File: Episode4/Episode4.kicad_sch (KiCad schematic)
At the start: 41 parts, among them J1 CARD, J10 CARD, J11 CARD, J12 CARD, J13 CARD, J14 CARD, J2 CARD, J3 CARD, J4 CARD, J5 CARD, J6 CARD, J7 BB Con, J8 ATX POWER, J9 CARD, SW1 POWER, U1 74HCT14, U2 74HCT74

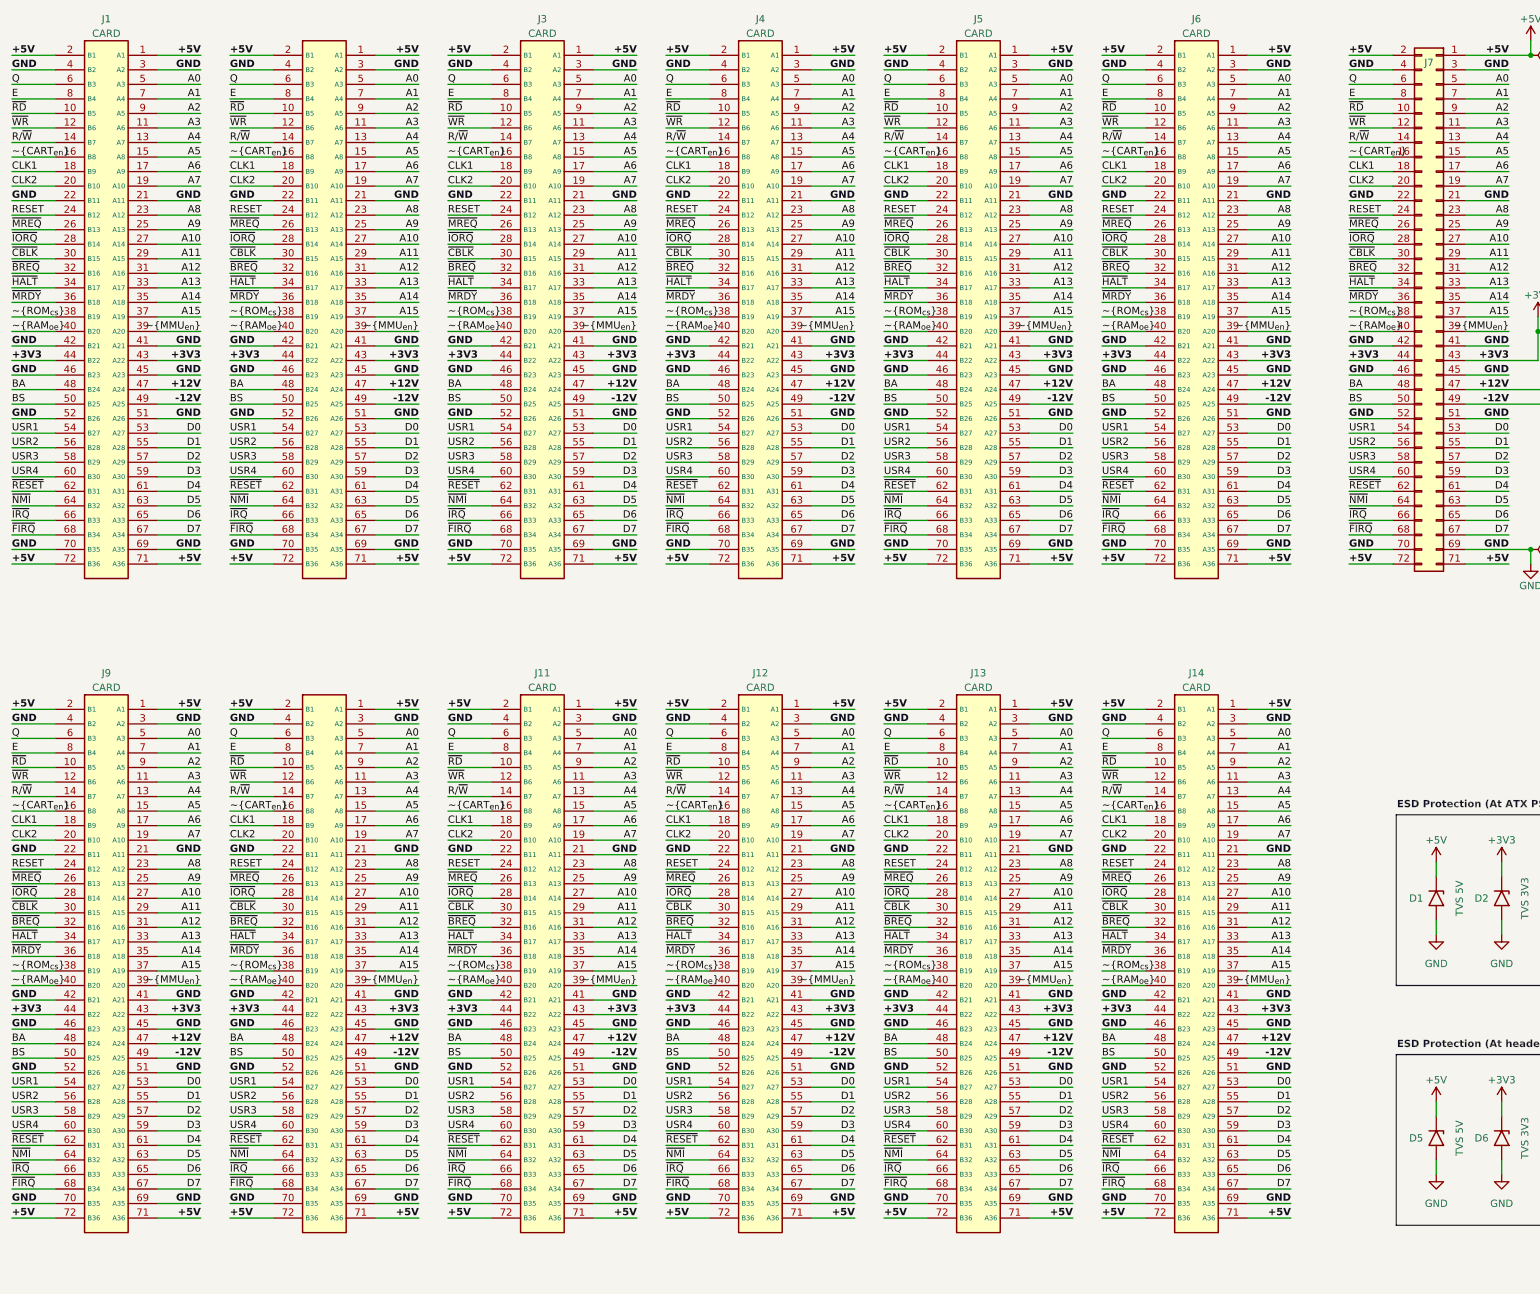
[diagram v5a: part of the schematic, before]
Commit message: Added various IRQ and FIRQ lines
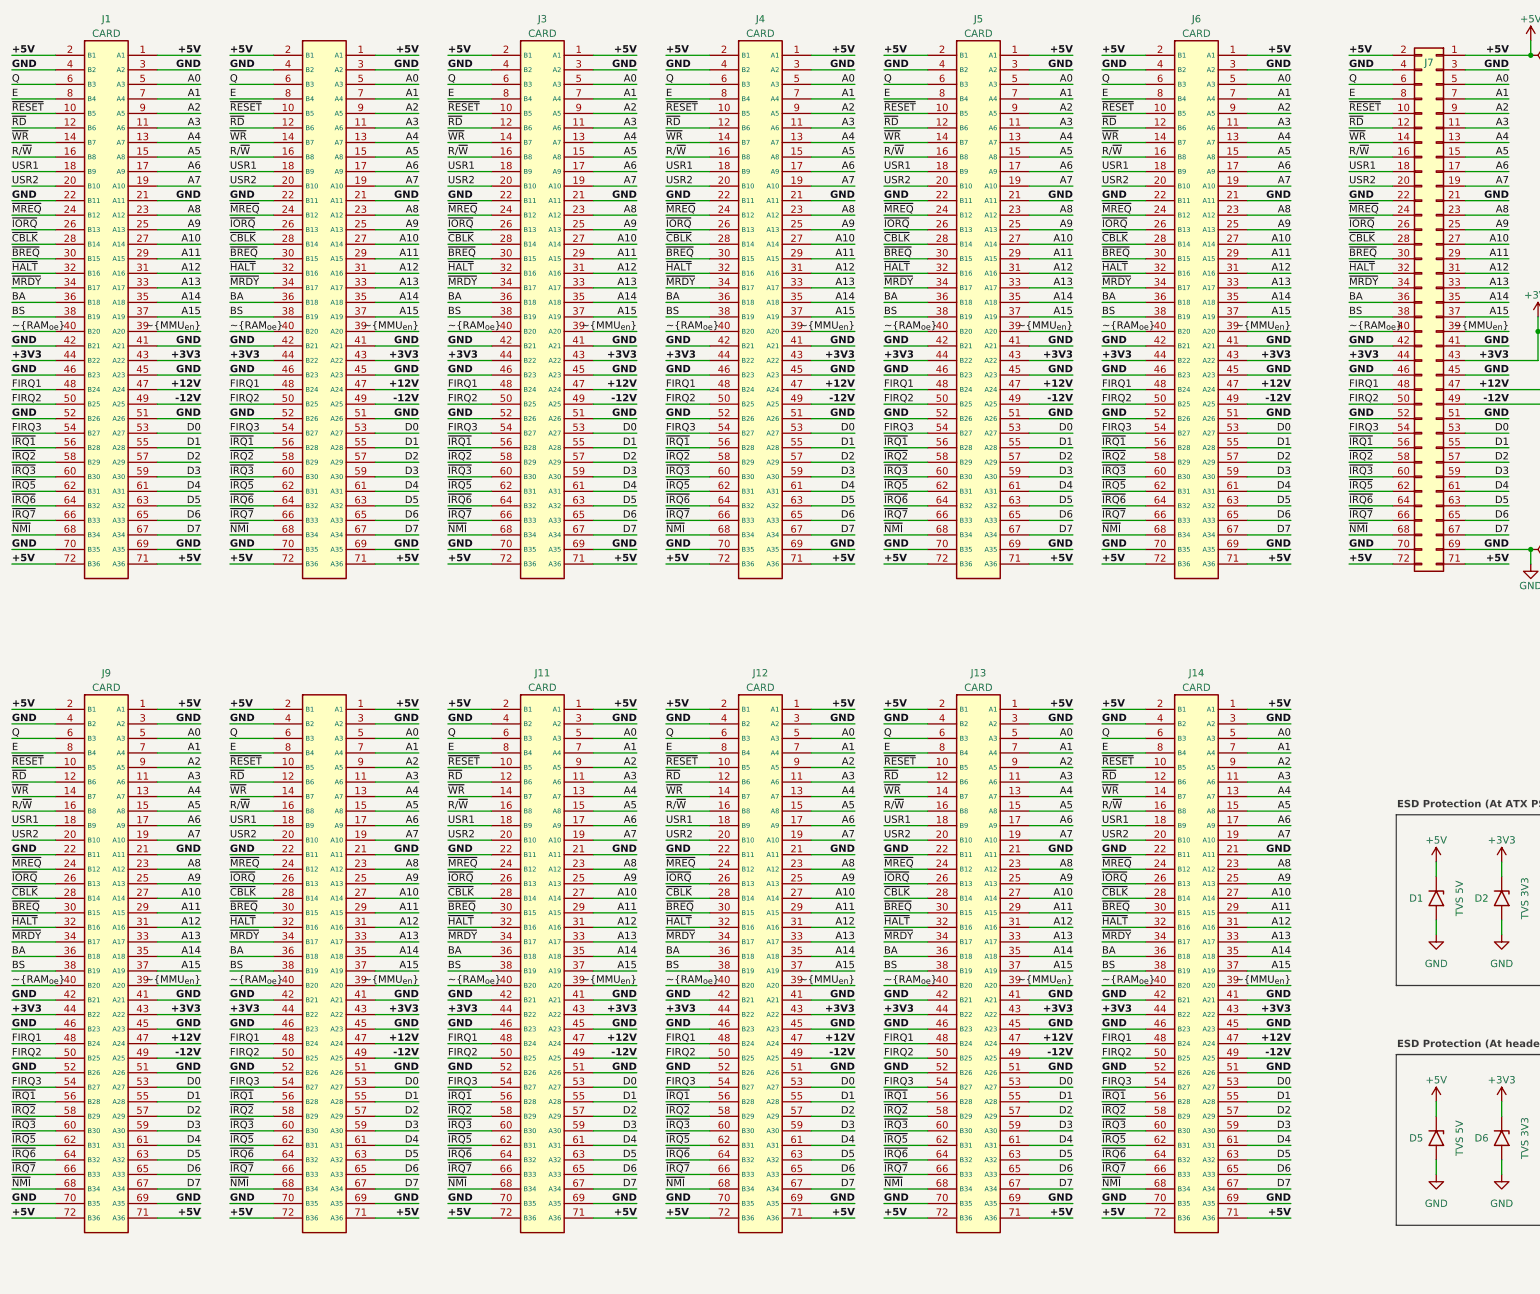
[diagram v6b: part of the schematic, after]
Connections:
- net CLK1 is gone; now on net USR1: J1.18 (B9), J10.18 (B9), J11.18 (B9), J12.18 (B9), J13.18 (B9), J14.18 (B9), J2.18 (B9), J3.18 (B9), J4.18 (B9), J5.18 (B9), J6.18 (B9), J7.18 (Pin_18), J9.18 (B9)
- net CLK2 is gone; now on net USR2: J1.20 (B10), J10.20 (B10), J11.20 (B10), J12.20 (B10), J13.20 (B10), J14.20 (B10), J2.20 (B10), J3.20 (B10), J4.20 (B10), J5.20 (B10), J6.20 (B10), J7.20 (Pin_20), J9.20 (B10)
- net RESET is gone; now on net ~{MREQ}: J1.24 (B12), J10.24 (B12), J11.24 (B12), J12.24 (B12), J13.24 (B12), J14.24 (B12), J2.24 (B12), J3.24 (B12), J4.24 (B12), J5.24 (B12), J6.24 (B12), J7.24 (Pin_24), J9.24 (B12)
- net ~{CART_{en}} is gone; now on net R/~{W}: J1.16 (B8), J10.16 (B8), J11.16 (B8), J12.16 (B8), J13.16 (B8), J14.16 (B8), J2.16 (B8), J3.16 (B8), J4.16 (B8), J5.16 (B8), J6.16 (B8), J7.16 (Pin_16), J9.16 (B8)
- net ~{FIRQ} is gone; now on net ~{NMI}: J1.68 (B34), J10.68 (B34), J11.68 (B34), J12.68 (B34), J13.68 (B34), J14.68 (B34), J2.68 (B34), J3.68 (B34), J4.68 (B34), J5.68 (B34), J6.68 (B34), J7.68 (Pin_68), J9.68 (B34)
- net ~{ROM_{cs}} is gone; now on net BS: J1.38 (B19), J10.38 (B19), J11.38 (B19), J12.38 (B19), J13.38 (B19), J14.38 (B19), J2.38 (B19), J3.38 (B19), J4.38 (B19), J5.38 (B19), J6.38 (B19), J7.38 (Pin_38), J9.38 (B19)
- net BA: now also J1.36 (B18), J10.36 (B18), J11.36 (B18), J12.36 (B18), J13.36 (B18), J14.36 (B18), J2.36 (B18), J3.36 (B18), J4.36 (B18), J5.36 (B18), J6.36 (B18), J7.36 (Pin_36), J9.36 (B18); no longer J1.48 (B24), J10.48 (B24), J11.48 (B24), J12.48 (B24), J13.48 (B24), J14.48 (B24), J2.48 (B24), J3.48 (B24), J4.48 (B24), J5.48 (B24), J6.48 (B24), J7.48 (Pin_48), J9.48 (B24)
- net BS: no longer J1.50 (B25), J10.50 (B25), J11.50 (B25), J12.50 (B25), J13.50 (B25), J14.50 (B25), J2.50 (B25), J3.50 (B25), J4.50 (B25), J5.50 (B25), J6.50 (B25), J7.50 (Pin_50), J9.50 (B25)
- net R/~{W}: no longer J1.14 (B7), J10.14 (B7), J11.14 (B7), J12.14 (B7), J13.14 (B7), J14.14 (B7), J2.14 (B7), J3.14 (B7), J4.14 (B7), J5.14 (B7), J6.14 (B7), J7.14 (Pin_14), J9.14 (B7)
- net USR1: no longer J1.54 (B27), J10.54 (B27), J11.54 (B27), J12.54 (B27), J13.54 (B27), J14.54 (B27), J2.54 (B27), J3.54 (B27), J4.54 (B27), J5.54 (B27), J6.54 (B27), J7.54 (Pin_54), J9.54 (B27)
- net USR2: no longer J1.56 (B28), J10.56 (B28), J11.56 (B28), J12.56 (B28), J13.56 (B28), J14.56 (B28), J2.56 (B28), J3.56 (B28), J4.56 (B28), J5.56 (B28), J6.56 (B28), J7.56 (Pin_56), J9.56 (B28)
- net ~{BREQ}: now also J1.30 (B15), J10.30 (B15), J11.30 (B15), J12.30 (B15), J13.30 (B15), J14.30 (B15), J2.30 (B15), J3.30 (B15), J4.30 (B15), J5.30 (B15), J6.30 (B15), J7.30 (Pin_30), J9.30 (B15); no longer J1.32 (B16), J10.32 (B16), J11.32 (B16), J12.32 (B16), J13.32 (B16), J14.32 (B16), J2.32 (B16), J3.32 (B16), J4.32 (B16), J5.32 (B16), J6.32 (B16), J7.32 (Pin_32), J9.32 (B16)
- net ~{CBLK}: now also J1.28 (B14), J10.28 (B14), J11.28 (B14), J12.28 (B14), J13.28 (B14), J14.28 (B14), J2.28 (B14), J3.28 (B14), J4.28 (B14), J5.28 (B14), J6.28 (B14), J7.28 (Pin_28), J9.28 (B14); no longer J1.30 (B15), J10.30 (B15), J11.30 (B15), J12.30 (B15), J13.30 (B15), J14.30 (B15), J2.30 (B15), J3.30 (B15), J4.30 (B15), J5.30 (B15), J6.30 (B15), J7.30 (Pin_30), J9.30 (B15)
- net ~{HALT}: now also J1.32 (B16), J10.32 (B16), J11.32 (B16), J12.32 (B16), J13.32 (B16), J14.32 (B16), J2.32 (B16), J3.32 (B16), J4.32 (B16), J5.32 (B16), J6.32 (B16), J7.32 (Pin_32), J9.32 (B16); no longer J1.34 (B17), J10.34 (B17), J11.34 (B17), J12.34 (B17), J13.34 (B17), J14.34 (B17), J2.34 (B17), J3.34 (B17), J4.34 (B17), J5.34 (B17), J6.34 (B17), J7.34 (Pin_34), J9.34 (B17)
- net ~{IORQ}: now also J1.26 (B13), J10.26 (B13), J11.26 (B13), J12.26 (B13), J13.26 (B13), J14.26 (B13), J2.26 (B13), J3.26 (B13), J4.26 (B13), J5.26 (B13), J6.26 (B13), J7.26 (Pin_26), J9.26 (B13); no longer J1.28 (B14), J10.28 (B14), J11.28 (B14), J12.28 (B14), J13.28 (B14), J14.28 (B14), J2.28 (B14), J3.28 (B14), J4.28 (B14), J5.28 (B14), J6.28 (B14), J7.28 (Pin_28), J9.28 (B14)
- net ~{MRDY}: now also J1.34 (B17), J10.34 (B17), J11.34 (B17), J12.34 (B17), J13.34 (B17), J14.34 (B17), J2.34 (B17), J3.34 (B17), J4.34 (B17), J5.34 (B17), J6.34 (B17), J7.34 (Pin_34), J9.34 (B17); no longer J1.36 (B18), J10.36 (B18), J11.36 (B18), J12.36 (B18), J13.36 (B18), J14.36 (B18), J2.36 (B18), J3.36 (B18), J4.36 (B18), J5.36 (B18), J6.36 (B18), J7.36 (Pin_36), J9.36 (B18)
- net ~{MREQ}: no longer J1.26 (B13), J10.26 (B13), J11.26 (B13), J12.26 (B13), J13.26 (B13), J14.26 (B13), J2.26 (B13), J3.26 (B13), J4.26 (B13), J5.26 (B13), J6.26 (B13), J7.26 (Pin_26), J9.26 (B13)
- net ~{NMI}: no longer J1.64 (B32), J10.64 (B32), J11.64 (B32), J12.64 (B32), J13.64 (B32), J14.64 (B32), J2.64 (B32), J3.64 (B32), J4.64 (B32), J5.64 (B32), J6.64 (B32), J7.64 (Pin_64), J9.64 (B32)
- net ~{RD}: now also J1.12 (B6), J10.12 (B6), J11.12 (B6), J12.12 (B6), J13.12 (B6), J14.12 (B6), J2.12 (B6), J3.12 (B6), J4.12 (B6), J5.12 (B6), J6.12 (B6), J7.12 (Pin_12), J9.12 (B6); no longer J1.10 (B5), J10.10 (B5), J11.10 (B5), J12.10 (B5), J13.10 (B5), J14.10 (B5), J2.10 (B5), J3.10 (B5), J4.10 (B5), J5.10 (B5), J6.10 (B5), J7.10 (Pin_10), J9.10 (B5)
- net ~{RESET}: now also J1.10 (B5), J10.10 (B5), J11.10 (B5), J12.10 (B5), J13.10 (B5), J14.10 (B5), J2.10 (B5), J3.10 (B5), J4.10 (B5), J5.10 (B5), J6.10 (B5), J7.10 (Pin_10), J9.10 (B5); no longer J1.62 (B31), J10.62 (B31), J11.62 (B31), J12.62 (B31), J13.62 (B31), J14.62 (B31), J2.62 (B31), J3.62 (B31), J4.62 (B31), J5.62 (B31), J6.62 (B31), J7.62 (Pin_62), J9.62 (B31)
- net ~{WR}: now also J1.14 (B7), J10.14 (B7), J11.14 (B7), J12.14 (B7), J13.14 (B7), J14.14 (B7), J2.14 (B7), J3.14 (B7), J4.14 (B7), J5.14 (B7), J6.14 (B7), J7.14 (Pin_14), J9.14 (B7); no longer J1.12 (B6), J10.12 (B6), J11.12 (B6), J12.12 (B6), J13.12 (B6), J14.12 (B6), J2.12 (B6), J3.12 (B6), J4.12 (B6), J5.12 (B6), J6.12 (B6), J7.12 (Pin_12), J9.12 (B6)
- net USR3 renamed ~{IRQ2}
- net USR4 renamed ~{IRQ3}
- net ~{IRQ} renamed ~{IRQ7}
- new net FIRQ1: J1.48 (B24), J10.48 (B24), J11.48 (B24), J12.48 (B24), J13.48 (B24), J14.48 (B24), J2.48 (B24), J3.48 (B24), J4.48 (B24), J5.48 (B24), J6.48 (B24), J7.48 (Pin_48), J9.48 (B24)
- new net FIRQ2: J1.50 (B25), J10.50 (B25), J11.50 (B25), J12.50 (B25), J13.50 (B25), J14.50 (B25), J2.50 (B25), J3.50 (B25), J4.50 (B25), J5.50 (B25), J6.50 (B25), J7.50 (Pin_50), J9.50 (B25)
- new net FIRQ3: J1.54 (B27), J10.54 (B27), J11.54 (B27), J12.54 (B27), J13.54 (B27), J14.54 (B27), J2.54 (B27), J3.54 (B27), J4.54 (B27), J5.54 (B27), J6.54 (B27), J7.54 (Pin_54), J9.54 (B27)
- new net ~{IRQ1}: J1.56 (B28), J10.56 (B28), J11.56 (B28), J12.56 (B28), J13.56 (B28), J14.56 (B28), J2.56 (B28), J3.56 (B28), J4.56 (B28), J5.56 (B28), J6.56 (B28), J7.56 (Pin_56), J9.56 (B28)
- new net ~{IRQ5}: J1.62 (B31), J10.62 (B31), J11.62 (B31), J12.62 (B31), J13.62 (B31), J14.62 (B31), J2.62 (B31), J3.62 (B31), J4.62 (B31), J5.62 (B31), J6.62 (B31), J7.62 (Pin_62), J9.62 (B31)
- new net ~{IRQ6}: J1.64 (B32), J10.64 (B32), J11.64 (B32), J12.64 (B32), J13.64 (B32), J14.64 (B32), J2.64 (B32), J3.64 (B32), J4.64 (B32), J5.64 (B32), J6.64 (B32), J7.64 (Pin_64), J9.64 (B32)

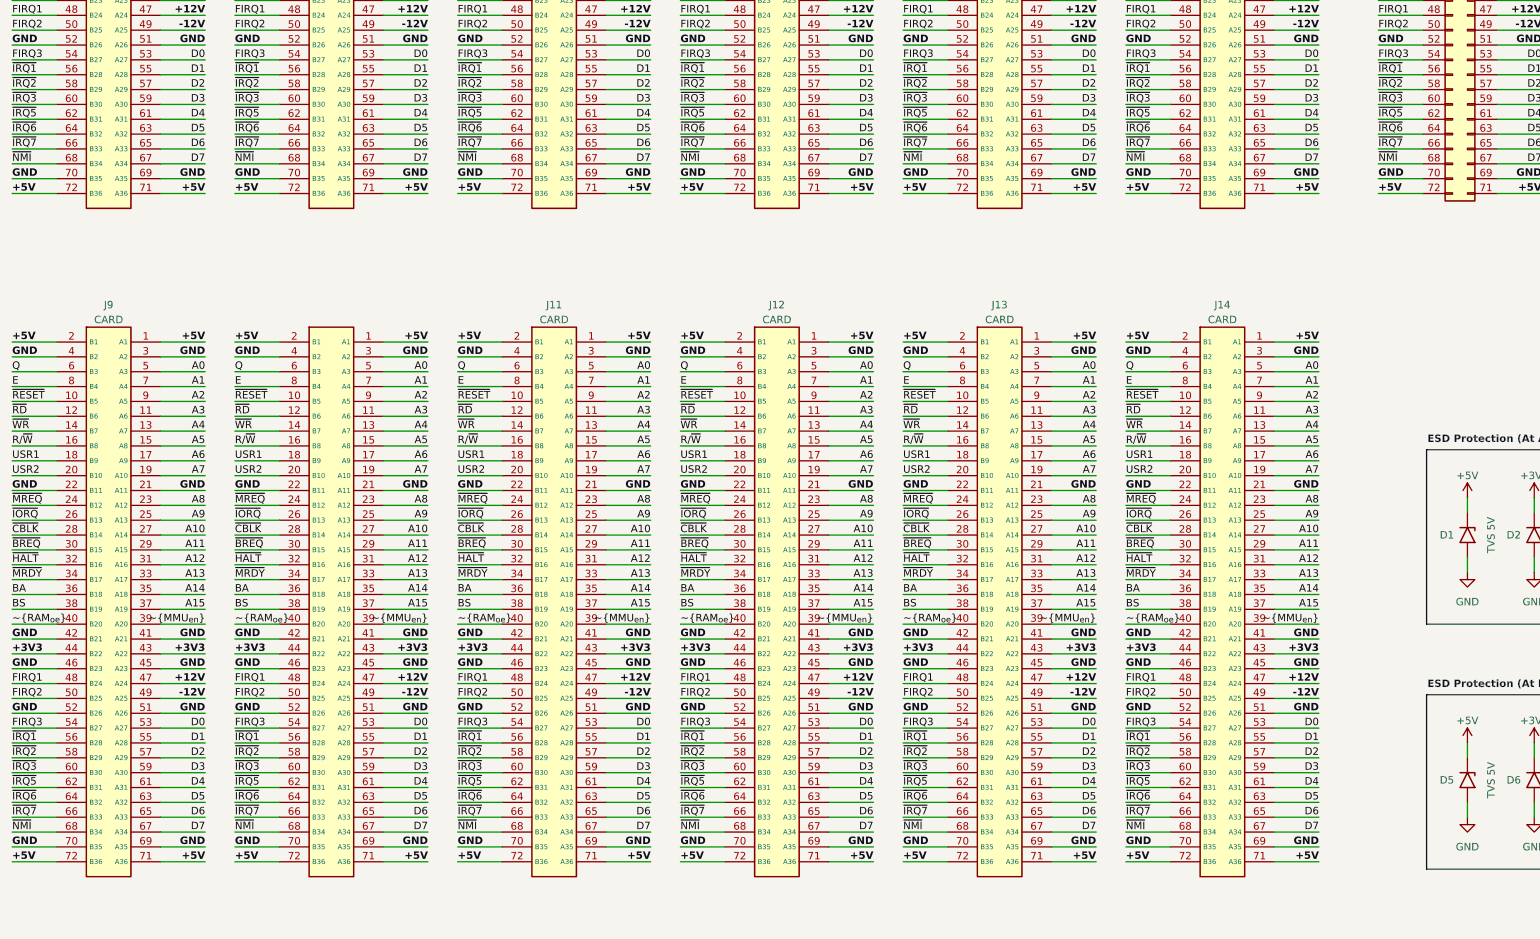
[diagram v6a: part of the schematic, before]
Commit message: Shuffled around IRQ numbers, and removed NMI, as it will by on the CPU card only.
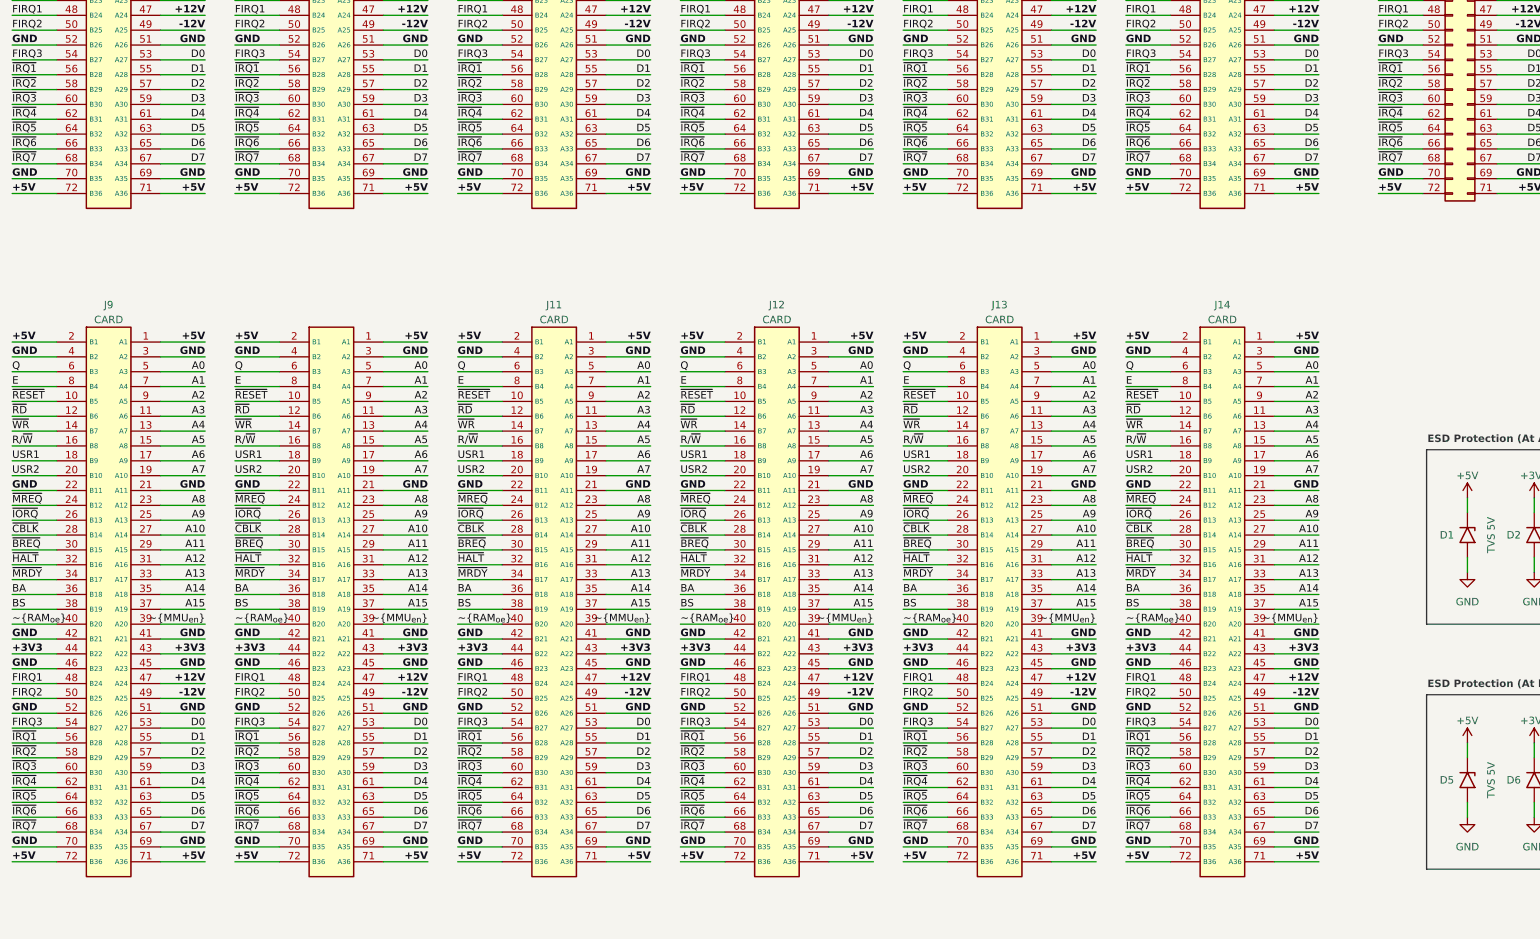
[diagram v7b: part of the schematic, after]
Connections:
- net ~{NMI} is gone; now on net ~{IRQ7}: J1.68 (B34), J10.68 (B34), J11.68 (B34), J12.68 (B34), J13.68 (B34), J14.68 (B34), J2.68 (B34), J3.68 (B34), J4.68 (B34), J5.68 (B34), J6.68 (B34), J7.68 (Pin_68), J9.68 (B34)
- net ~{IRQ5}: now also J1.64 (B32), J10.64 (B32), J11.64 (B32), J12.64 (B32), J13.64 (B32), J14.64 (B32), J2.64 (B32), J3.64 (B32), J4.64 (B32), J5.64 (B32), J6.64 (B32), J7.64 (Pin_64), J9.64 (B32); no longer J1.62 (B31), J10.62 (B31), J11.62 (B31), J12.62 (B31), J13.62 (B31), J14.62 (B31), J2.62 (B31), J3.62 (B31), J4.62 (B31), J5.62 (B31), J6.62 (B31), J7.62 (Pin_62), J9.62 (B31)
- net ~{IRQ6}: now also J1.66 (B33), J10.66 (B33), J11.66 (B33), J12.66 (B33), J13.66 (B33), J14.66 (B33), J2.66 (B33), J3.66 (B33), J4.66 (B33), J5.66 (B33), J6.66 (B33), J7.66 (Pin_66), J9.66 (B33); no longer J1.64 (B32), J10.64 (B32), J11.64 (B32), J12.64 (B32), J13.64 (B32), J14.64 (B32), J2.64 (B32), J3.64 (B32), J4.64 (B32), J5.64 (B32), J6.64 (B32), J7.64 (Pin_64), J9.64 (B32)
- net ~{IRQ7}: no longer J1.66 (B33), J10.66 (B33), J11.66 (B33), J12.66 (B33), J13.66 (B33), J14.66 (B33), J2.66 (B33), J3.66 (B33), J4.66 (B33), J5.66 (B33), J6.66 (B33), J7.66 (Pin_66), J9.66 (B33)
- new net ~{IRQ4}: J1.62 (B31), J10.62 (B31), J11.62 (B31), J12.62 (B31), J13.62 (B31), J14.62 (B31), J2.62 (B31), J3.62 (B31), J4.62 (B31), J5.62 (B31), J6.62 (B31), J7.62 (Pin_62), J9.62 (B31)
